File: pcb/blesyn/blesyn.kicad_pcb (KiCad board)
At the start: 2 copper layers, 17.8 x 35.6 mm, 11 parts, among them J1 RJ12, U1 XIAO-ESP32-S3, U2 R-783.3-0.5

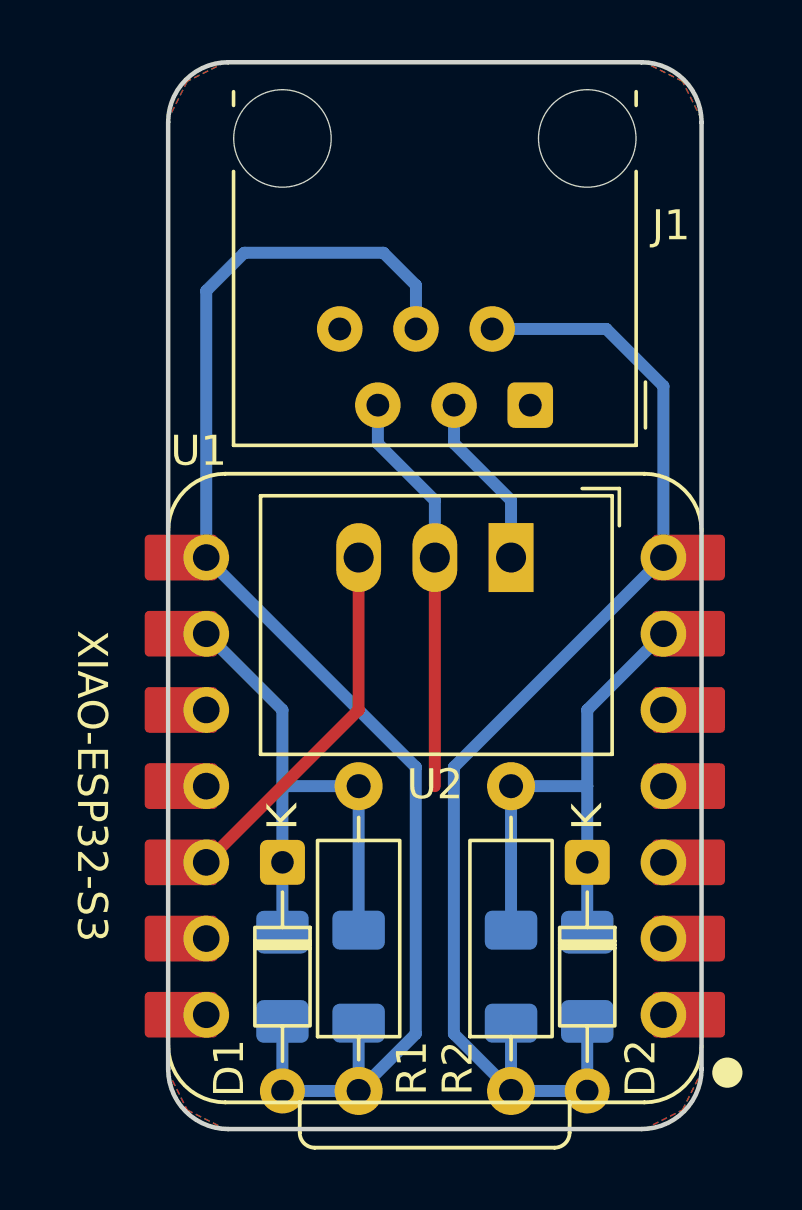
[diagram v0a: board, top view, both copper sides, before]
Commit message: board widen 50 mil at each side, 100 mil (2.54 mm) total to enter rails in 3D printed enclosure
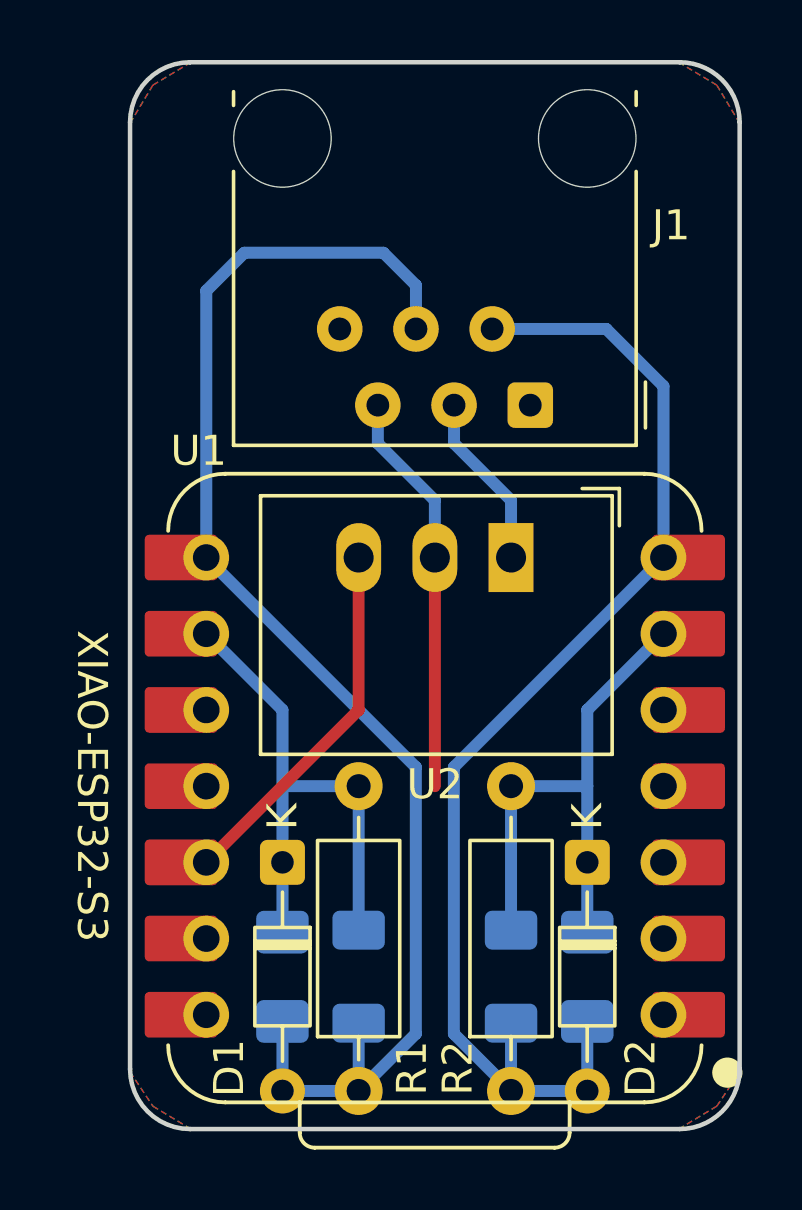
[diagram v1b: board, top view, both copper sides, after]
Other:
- board size 17.8 x 35.6 mm -> 20.3 x 35.6 mm
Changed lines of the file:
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@@
 	)
 	(paper "A4")
+	(title_block
+		(date "2026-09-03")
+		(rev "1.1")
+	)
 	(layers
 		(0 "F.Cu" signal)
@@
 	)
 	(gr_arc
-		(start 55 111.439964)
-		(mid 55.585786 110.02575)
-		(end 57 109.439964)
+		(start 53.73 111.439964)
+		(mid 54.315799 110.025774)
+		(end 55.73 109.439964)
 		(stroke
 			(width 0.15)
@@
 	)
 	(gr_line
-		(start 55 142.999964)
-		(end 55 111.439964)
+		(start 53.73 142.999964)
+		(end 53.73 111.439964)
 		(stroke
 			(width 0.15)
@@
 	)
 	(gr_line
-		(start 57 109.439964)
-		(end 70.78 109.439964)
+		(start 55.73 109.439964)
+		(end 72.05 109.439964)
 		(stroke
 			(width 0.15)
@@
 	)
 	(gr_arc
-		(start 57 144.999964)
-		(mid 55.585786 144.414178)
-		(end 55 142.999964)
+		(start 55.73 144.999964)
+		(mid 54.315799 144.414175)
+		(end 53.73 142.999964)
 		(stroke
 			(width 0.15)
@@
 	)
 	(gr_arc
-		(start 70.78 109.439964)
-		(mid 72.194214 110.02575)
-		(end 72.78 111.439964)
+		(start 72.05 109.439964)
+		(mid 73.464214 110.02575)
+		(end 74.05 111.439964)
 		(stroke
 			(width 0.15)
@@
 	)
 	(gr_line
-		(start 70.78 144.999964)
-		(end 57 144.999964)
+		(start 72.05 144.999964)
+		(end 55.73 144.999964)
 		(stroke
 			(width 0.15)
@@
 	)
 	(gr_line
-		(start 72.78 111.439964)
-		(end 72.78 142.999964)
+		(start 74.05 111.439964)
+		(end 74.05 142.999964)
 		(stroke
 			(width 0.15)
@@
 	)
 	(gr_arc
-		(start 72.78 142.999964)
-		(mid 72.194226 144.414201)
-		(end 70.78 144.999964)
+		(start 74.05 142.999964)
+		(mid 73.464226 144.414201)
+		(end 72.05 144.999964)
 		(stroke
 			(width 0.15)
@@
 		(polygon
 			(pts
-				(xy 56.905 109.44) (xy 55.635 110.075) (xy 55 111.345) (xy 55 143.095) (xy 55.635 144.365) (xy 56.905 145)
-				(xy 70.875 145) (xy 72.145 144.365) (xy 72.78 143.095) (xy 72.78 111.345) (xy 72.145 110.075) (xy 70.875 109.44)
+				(xy 55.762 109.44) (xy 54.492 110.202) (xy 53.73 111.472) (xy 53.73 143.095) (xy 54.492 144.238)
+				(xy 55.762 145) (xy 72.018 145) (xy 73.288 144.238) (xy 74.05 143.095) (xy 74.05 111.472) (xy 73.288 110.202)
+				(xy 72.018 109.44)
 			)
 		)
@@
 		(polygon
 			(pts
-				(xy 56.905 109.44) (xy 55.635 110.075) (xy 55 111.345) (xy 55 143.095) (xy 55.635 144.365) (xy 56.905 145)
-				(xy 70.875 145) (xy 72.145 144.365) (xy 72.78 143.095) (xy 72.78 111.345) (xy 72.145 110.075) (xy 70.875 109.44)
+				(xy 55.762 109.44) (xy 54.492 110.202) (xy 53.73 111.472) (xy 53.73 143.095) (xy 54.492 144.238)
+				(xy 55.762 145) (xy 72.018 145) (xy 73.288 144.238) (xy 74.05 143.095) (xy 74.05 111.472) (xy 73.288 110.202)
+				(xy 72.018 109.44)
 			)
 		)

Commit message: version v1.1 on silkscreen
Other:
- board text added: "v1.1"
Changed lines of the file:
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@@
 		(tags "RJ12 connector")
 		(property "Reference" "J1"
-			(at -4.694 5.992 0)
+			(at -4.694 8.89 0)
 			(layer "F.SilkS")
 			(effects
@@
 		(layer "Edge.Cuts")
 	)
+	(gr_text "v1.1"
+		(at 72.78 118.33 90)
+		(layer "F.SilkS")
+		(effects
+			(font
+				(size 1 1)
+				(thickness 0.15)
+			)
+			(justify left bottom)
+		)
+	)
 	(segment

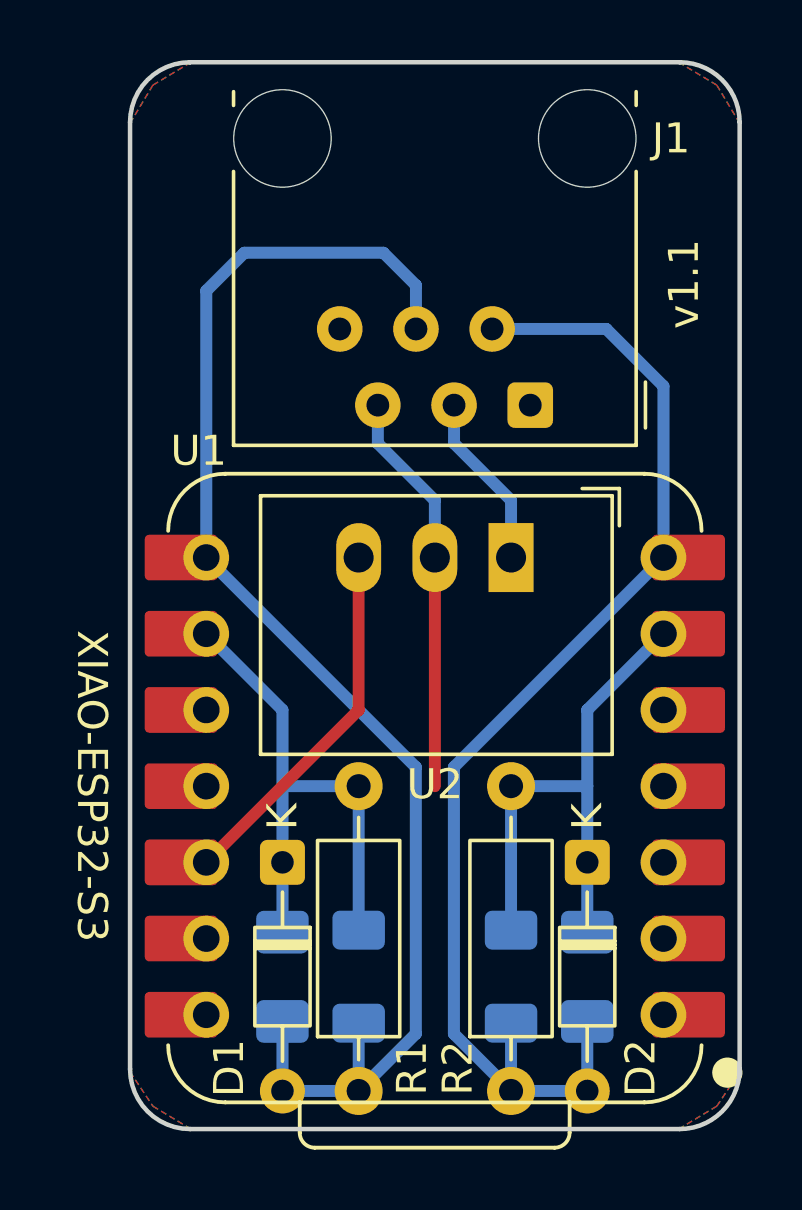
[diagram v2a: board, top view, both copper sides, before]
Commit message: pcb 1.2 shrinked back
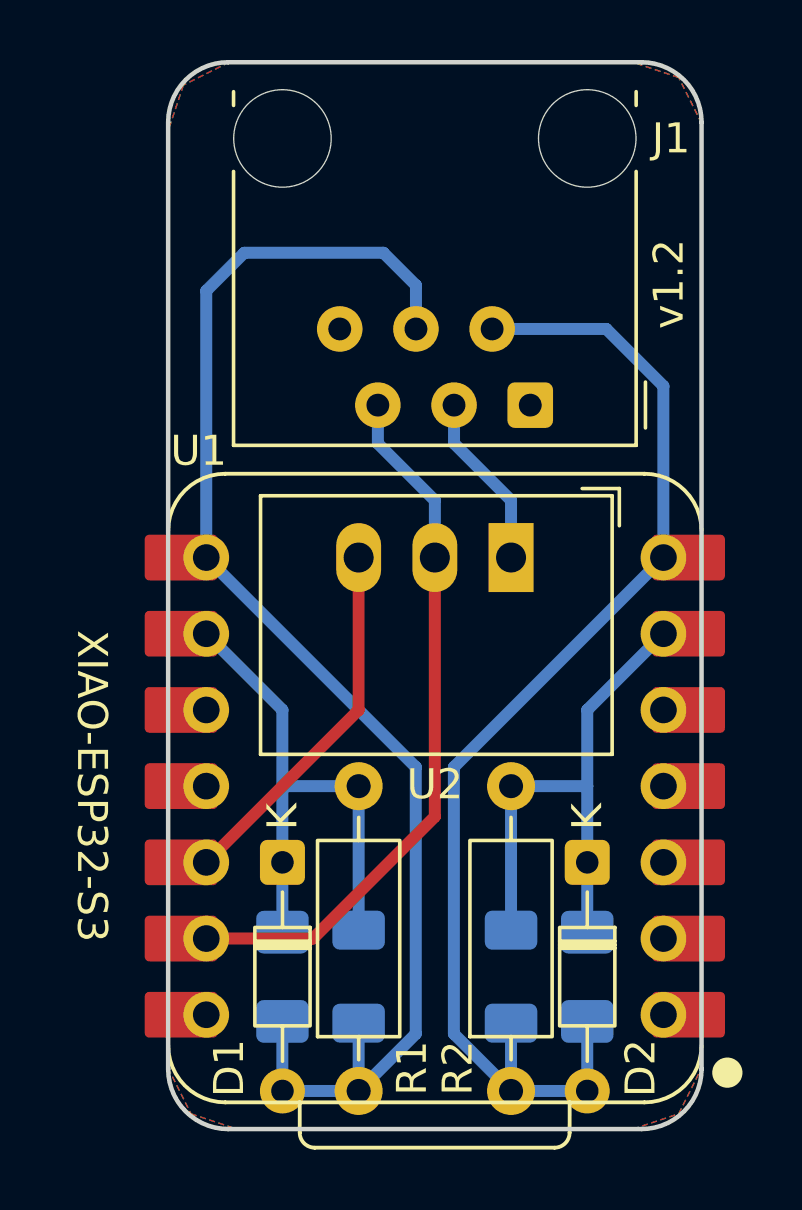
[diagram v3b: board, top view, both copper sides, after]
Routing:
- net GND: track 13.5 -> 23.8 mm
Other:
- board size 20.3 x 35.6 mm -> 17.8 x 35.6 mm
- board text added: "v1.2"
- board text removed: "v1.1"
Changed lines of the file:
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@@
 	(paper "A4")
 	(title_block
-		(date "2026-09-03")
-		(rev "1.1")
+		(date "2026-09-07")
+		(rev "1.2")
 	)
 	(layers
@@
 	)
 	(gr_arc
-		(start 53.73 111.439964)
-		(mid 54.315799 110.025774)
-		(end 55.73 109.439964)
+		(start 55 111.439964)
+		(mid 55.585793 110.025738)
+		(end 57 109.439964)
 		(stroke
 			(width 0.15)
@@
 	)
 	(gr_line
-		(start 53.73 142.999964)
-		(end 53.73 111.439964)
+		(start 55 143)
+		(end 55 111.44)
 		(stroke
 			(width 0.15)
@@
 	)
 	(gr_line
-		(start 55.73 109.439964)
-		(end 72.05 109.439964)
+		(start 57 109.439964)
+		(end 70.78 109.439964)
 		(stroke
 			(width 0.15)
@@
 	)
 	(gr_arc
-		(start 55.73 144.999964)
-		(mid 54.315799 144.414175)
-		(end 53.73 142.999964)
+		(start 57 144.999964)
+		(mid 55.585764 144.414181)
+		(end 55 142.999964)
 		(stroke
 			(width 0.15)
@@
 	)
 	(gr_arc
-		(start 72.05 109.439964)
-		(mid 73.464214 110.02575)
-		(end 74.05 111.439964)
+		(start 70.78 109.439964)
+		(mid 72.194226 110.025748)
+		(end 72.78 111.439964)
 		(stroke
 			(width 0.15)
@@
 	)
 	(gr_line
-		(start 72.05 144.999964)
-		(end 55.73 144.999964)
+		(start 70.78 144.999964)
+		(end 57 144.999964)
 		(stroke
 			(width 0.15)
@@
 	)
 	(gr_line
-		(start 74.05 111.439964)
-		(end 74.05 142.999964)
+		(start 72.78 111.439964)
+		(end 72.78 142.999964)
 		(stroke
 			(width 0.15)
@@
 	)
 	(gr_arc
-		(start 74.05 142.999964)
-		(mid 73.464226 144.414201)
-		(end 72.05 144.999964)
+		(start 72.78 142.999964)
+		(mid 72.194226 144.414201)
+		(end 70.78 144.999964)
 		(stroke
 			(width 0.15)
@@
 		(layer "Edge.Cuts")
 	)
-	(gr_text "v1.1"
-		(at 72.78 118.33 90)
+	(gr_text "v1.2"
+		(at 72.272 118.33 90)
 		(layer "F.SilkS")
 		(effects
@@
 	)
 	(segment
-		(start 63.89 125.95)
-		(end 63.89 133.57)
+		(start 59.826 138.65)
+		(end 63.89 134.586)
+		(width 0.4)
+		(layer "F.Cu")
+		(net "GND")
+	)
+	(segment
+		(start 63.89 134.586)
+		(end 63.89 125.95)
+		(width 0.4)
+		(layer "F.Cu")
+		(net "GND")
+	)
+	(segment
+		(start 56.27 138.65)
+		(end 59.826 138.65)
 		(width 0.4)
 		(layer "F.Cu")
@@
 		(polygon
 			(pts
-				(xy 55.762 109.44) (xy 54.492 110.202) (xy 53.73 111.472) (xy 53.73 143.095) (xy 54.492 144.238)
-				(xy 55.762 145) (xy 72.018 145) (xy 73.288 144.238) (xy 74.05 143.095) (xy 74.05 111.472) (xy 73.288 110.202)
-				(xy 72.018 109.44)
+				(xy 57.032 109.44) (xy 55.508 110.202) (xy 55 111.726) (xy 55 142.968) (xy 55.762 144.492) (xy 57.286 145)
+				(xy 70.494 145) (xy 72.018 144.492) (xy 72.78 142.968) (xy 72.78 111.472) (xy 72.018 109.948) (xy 70.494 109.44)
 			)
 		)
@@
 		(polygon
 			(pts
-				(xy 55.762 109.44) (xy 54.492 110.202) (xy 53.73 111.472) (xy 53.73 143.095) (xy 54.492 144.238)
-				(xy 55.762 145) (xy 72.018 145) (xy 73.288 144.238) (xy 74.05 143.095) (xy 74.05 111.472) (xy 73.288 110.202)
-				(xy 72.018 109.44)
+				(xy 57.032 109.44) (xy 55.508 110.202) (xy 55 111.726) (xy 55 142.968) (xy 55.762 144.492) (xy 57.286 145)
+				(xy 70.494 145) (xy 72.018 144.492) (xy 72.78 142.968) (xy 72.78 111.472) (xy 72.018 109.948) (xy 70.494 109.44)
 			)
 		)
